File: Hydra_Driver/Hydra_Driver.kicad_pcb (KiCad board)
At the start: 2 copper layers, 58 x 42 mm, 99 parts, among them IC101 ESP32-S3-WROOM-1-N4, IC201 DRV8313RHHR, IC301 DRV8313RHHR, J101 USB4105-GF-A, J102 Conn_01x02, J103 Conn_01x07, J104 Conn_01x04, J105 Conn_01x03, J107 Conn_01x04, J108 Conn_01x03, J109 Conn_01x02, J110 Conn_01x07, SW101 SW_SPST, SW102 SW_SPST, U101 USBLC6-2SC6, U102 MIC5504-3.3YM5-TR, U103 SN74LVC1G80DBVR, U201 INA4181A2IPWR, U301 INA4181A2IPWR

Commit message: Added thermal vias to driver pads
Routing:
- net GND: track 167.0 -> 170.9 mm, vias 65 -> 73
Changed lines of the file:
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@@
+	)
+	(segment
+		(start 43.66 18.89)
+		(end 44.02 19.25)
+		(width 0.2)
+		(layer "F.Cu")
+		(net 1)
 	)
 	(segment
@@
 	)
 	(segment
+		(start 42.1 19.25)
+		(end 43.3 19.25)
+		(width 0.2)
+		(layer "F.Cu")
+		(net 1)
+	)
+	(segment
 		(start 55.4625 24.75)
 		(end 54.603 24.75)
@@
 	)
 	(segment
+		(start 44.168191 19.25)
+		(end 45.168191 20.25)
+		(width 0.2)
+		(layer "F.Cu")
+		(net 1)
+	)
+	(segment
 		(start 20.5 28.5)
 		(end 20.18 28.82)
@@
 	)
 	(segment
+		(start 46.4 21.6)
+		(end 46.69 21.31)
+		(width 0.2)
+		(layer "F.Cu")
+		(net 1)
+	)
+	(segment
+		(start 46 19.25)
+		(end 45.725 19.525)
+		(width 0.2)
+		(layer "F.Cu")
+		(net 1)
+	)
+	(segment
 		(start 20.18 13.43)
 		(end 20.5 13.75)
@@
 		(start 54.5 15.5)
 		(end 54.75 15.25)
+		(width 0.2)
+		(layer "F.Cu")
+		(net 1)
+	)
+	(segment
+		(start 43.5 19.75)
+		(end 44.5 19.75)
 		(width 0.2)
 		(layer "F.Cu")
@@
 	)
 	(segment
+		(start 46.35 21.6)
+		(end 45 20.25)
+		(width 0.2)
+		(layer "F.Cu")
+		(net 1)
+	)
+	(segment
 		(start 54.889 31.389)
 		(end 54.3 30.8)
@@
 	)
 	(segment
-		(start 46.5 17.35)
-		(end 46.5 18.75)
+		(start 44.02 19.25)
+		(end 44.168191 19.25)
 		(width 0.2)
 		(layer "F.Cu")
@@
 	(segment
 		(start 42.1 19.75)
-		(end 44.5 19.75)
+		(end 43.5 19.75)
 		(width 0.2)
 		(layer "F.Cu")
@@
 	)
 	(segment
+		(start 46.39 18.86)
+		(end 46.5 18.75)
+		(width 0.2)
+		(layer "F.Cu")
+		(net 1)
+	)
+	(segment
 		(start 54.3 30.8)
 		(end 54.3 30)
@@
 	)
 	(segment
+		(start 46.39 18.88)
+		(end 46.39 18.55)
+		(width 0.2)
+		(layer "F.Cu")
+		(net 1)
+	)
+	(segment
 		(start 54.603 24.75)
 		(end 54.603 24.2517)
@@
 	)
 	(segment
-		(start 46 19.25)
-		(end 45 20.25)
-		(width 0.2)
-		(layer "F.Cu")
-		(net 1)
-	)
-	(segment
 		(start 29.239728 34.85267)
 		(end 29.6174 34.474998)
@@
 	)
 	(segment
+		(start 46.5 18.44)
+		(end 46.5 17.35)
+		(width 0.2)
+		(layer "F.Cu")
+		(net 1)
+	)
+	(segment
 		(start 29.101415 34.85267)
 		(end 29.239728 34.85267)
@@
 		(start 36.9046 1.49)
 		(end 36.9046 0.9)
-		(width 0.2)
-		(layer "F.Cu")
-		(net 1)
-	)
-	(segment
-		(start 44 19.25)
-		(end 45 20.25)
 		(width 0.2)
 		(layer "F.Cu")
@@
 	)
 	(segment
+		(start 46.69 18.94)
+		(end 46.5 18.75)
+		(width 0.2)
+		(layer "F.Cu")
+		(net 1)
+	)
+	(segment
 		(start 46.5 16.50826)
 		(end 46.49587 16.50413)
@@
 	)
 	(segment
+		(start 46.39 18.88)
+		(end 46.39 18.86)
+		(width 0.2)
+		(layer "F.Cu")
+		(net 1)
+	)
+	(segment
 		(start 54.6 19.4)
 		(end 54.75 19.25)
@@
 	)
 	(segment
-		(start 46.5 18.75)
-		(end 45 20.25)
-		(width 0.2)
-		(layer "F.Cu")
-		(net 1)
-	)
-	(segment
 		(start 49.25 27.4)
 		(end 50.15 27.4)
@@
 	)
 	(segment
+		(start 46.4 21.6)
+		(end 46.35 21.6)
+		(width 0.2)
+		(layer "F.Cu")
+		(net 1)
+	)
+	(segment
 		(start 56 39.6)
 		(end 56.029 39.629)
@@
 	)
 	(segment
+		(start 43.3 19.25)
+		(end 43.66 18.89)
+		(width 0.2)
+		(layer "F.Cu")
+		(net 1)
+	)
+	(segment
+		(start 45.725 19.525)
+		(end 45 20.25)
+		(width 0.2)
+		(layer "F.Cu")
+		(net 1)
+	)
+	(segment
 		(start 10.62 17.244033)
 		(end 11.002 17.626033)
@@
 		(start 7 30)
 		(end 6.6 30.4)
-		(width 0.2)
-		(layer "F.Cu")
-		(net 1)
-	)
-	(segment
-		(start 42.1 19.25)
-		(end 44 19.25)
 		(width 0.2)
 		(layer "F.Cu")
@@
 	)
 	(segment
+		(start 45.168191 20.25)
+		(end 45 20.25)
+		(width 0.2)
+		(layer "F.Cu")
+		(net 1)
+	)
+	(segment
 		(start 57.699 24.199)
 		(end 57.699 26.311)
@@
 	)
 	(segment
+		(start 46.69 21.31)
+		(end 46.69 18.94)
+		(width 0.2)
+		(layer "F.Cu")
+		(net 1)
+	)
+	(segment
 		(start 52.9485 4.249999)
 		(end 51.5 4.25)
@@
 	)
 	(segment
+		(start 46.39 18.55)
+		(end 46.5 18.44)
+		(width 0.2)
+		(layer "F.Cu")
+		(net 1)
+	)
+	(segment
 		(start 5 23.214013)
 		(end 5.114013 23.1)
@@
 	(via
 		(at 48.335707 6.334293)
+		(size 0.6)
+		(drill 0.3)
+		(layers "F.Cu" "B.Cu")
+		(net 1)
+	)
+	(via
+		(at 46.26 32.3)
 		(size 0.6)
 		(drill 0.3)
@@
 	)
 	(via
+		(at 46.39 18.88)
+		(size 0.6)
+		(drill 0.3)
+		(layers "F.Cu" "B.Cu")
+		(net 1)
+	)
+	(via
 		(at 50.5 14.5)
 		(size 0.6)
@@
 	)
 	(via
+		(at 43.66 18.89)
+		(size 0.6)
+		(drill 0.3)
+		(layers "F.Cu" "B.Cu")
+		(net 1)
+	)
+	(via
 		(at 13.75 13.5)
 		(size 0.6)
@@
 	(via
 		(at 50.25 27.5)
+		(size 0.6)
+		(drill 0.3)
+		(layers "F.Cu" "B.Cu")
+		(net 1)
+	)
+	(via
+		(at 43.69 34.98)
 		(size 0.6)
 		(drill 0.3)
@@
 	)
 	(via
+		(at 46.28 34.92)
+		(size 0.6)
+		(drill 0.3)
+		(layers "F.Cu" "B.Cu")
+		(net 1)
+	)
+	(via
 		(at 50 8.25)
 		(size 0.6)
@@
 	(via
 		(at 36.6 40.4)
+		(size 0.6)
+		(drill 0.3)
+		(layers "F.Cu" "B.Cu")
+		(net 1)
+	)
+	(via
+		(at 46.4 21.6)
 		(size 0.6)
 		(drill 0.3)
@@
 		(size 0.6)
 		(drill 0.3)
+		(layers "F.Cu" "B.Cu")
+		(net 1)
+	)
+	(via
+		(at 43.64 21.66)
+		(size 0.6)
+		(drill 0.3)
+		(layers "F.Cu" "B.Cu")
+		(net 1)
+	)
+	(via
+		(at 43.7 32.36)
+		(size 0.6)
+		(drill 0.3)

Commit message: Incorporated design review feedback and updated fab files
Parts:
- C203, C204, C205, C303, C304, C305: value 1n -> 22n
- R201, R202, R203, R204, R205, R206, R301, R302, R303, R304, R305, R306: value 47 -> 10
- U201, U301: value INA4181A2IPWR -> INA4181A3IPWR
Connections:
- C208 pad 2: +3.3V -> /Driver_Unit/L3V3
- C210 pad 2: +3.3V -> /Driver_Unit/L3V3
- C308 pad 2: +3.3V -> /Driver_Unit1/L3V3
- C310 pad 2: +3.3V -> /Driver_Unit1/L3V3
- IC201 pad 25: +3.3V -> /Driver_Unit/L3V3
- IC301 pad 25: +3.3V -> /Driver_Unit1/L3V3
- R207 pad 2: +3.3V -> /Driver_Unit/L3V3
- R208 pad 2: +3.3V -> /Driver_Unit/L3V3
- R209 pad 2: +3.3V -> /Driver_Unit/L3V3
- R210 pad 2: +3.3V -> /Driver_Unit/L3V3
- R307 pad 2: +3.3V -> /Driver_Unit1/L3V3
- R308 pad 2: +3.3V -> /Driver_Unit1/L3V3
- R309 pad 2: +3.3V -> /Driver_Unit1/L3V3
- R310 pad 2: +3.3V -> /Driver_Unit1/L3V3
- U201 pad 5: +3.3V -> /Driver_Unit/L3V3
- U301 pad 5: +3.3V -> /Driver_Unit1/L3V3
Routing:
- net +3.3V: track 161.3 -> 113.0 mm, vias 8 -> 5
- net /Driver_Unit1/L3V3: track 0.00 -> 27.9 mm, vias 0 -> 2
- net /Driver_Unit/L3V3: track 0.00 -> 25.0 mm, vias 0 -> 2
- net /IN1A: track 13.7 -> 14.7 mm
- net /SENSE1A: track 13.6 -> 12.8 mm
- net /GPIO0: track 24.7 -> 25.4 mm
- net /SDA1: track 21.2 -> 21.8 mm
- net VMOT: track 177.6 -> 177.1 mm
- net GND: track 170.9 -> 171.2 mm, vias 73 -> 80
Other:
- board text added: "Hydra V2 ©CGR"

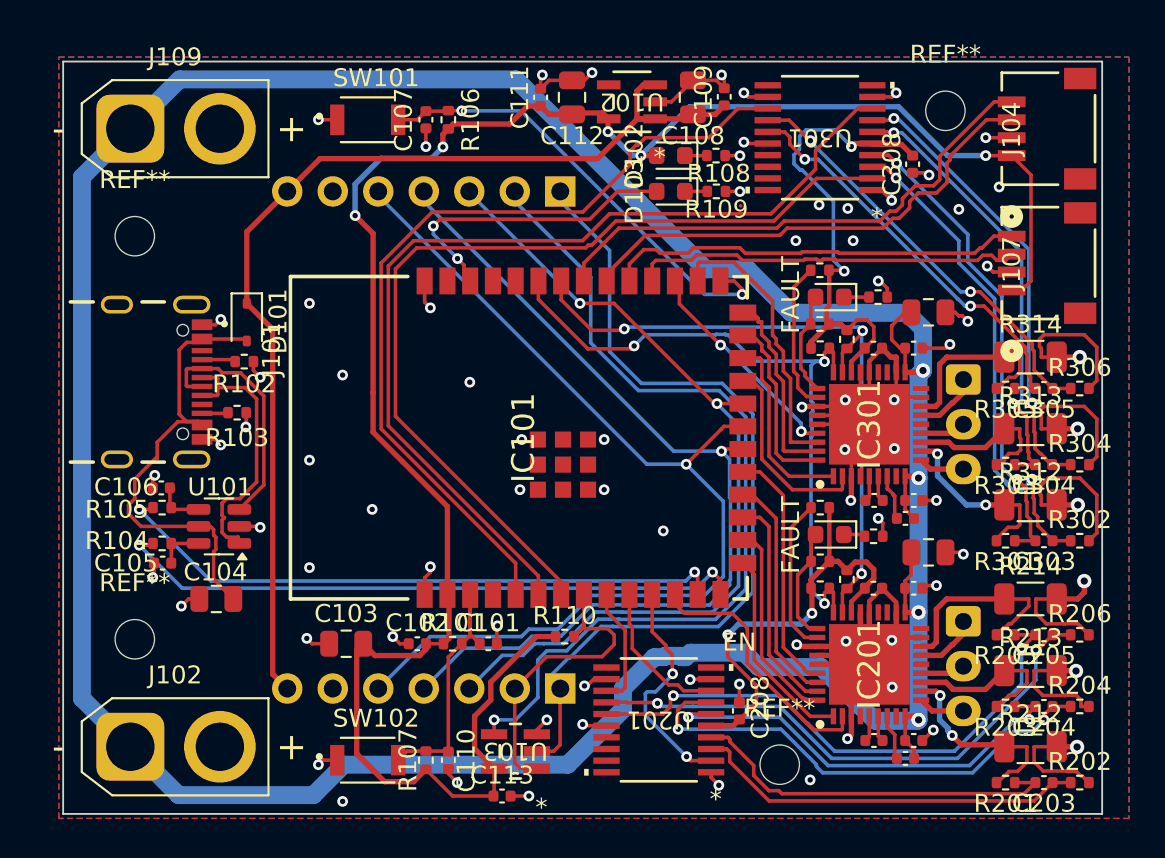
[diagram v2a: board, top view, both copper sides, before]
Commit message: Fixed issues preparing for build
Fixed XT30 connectors on Hydra_Driver reversed, fixed I2C connector pin order, refined silkscreens
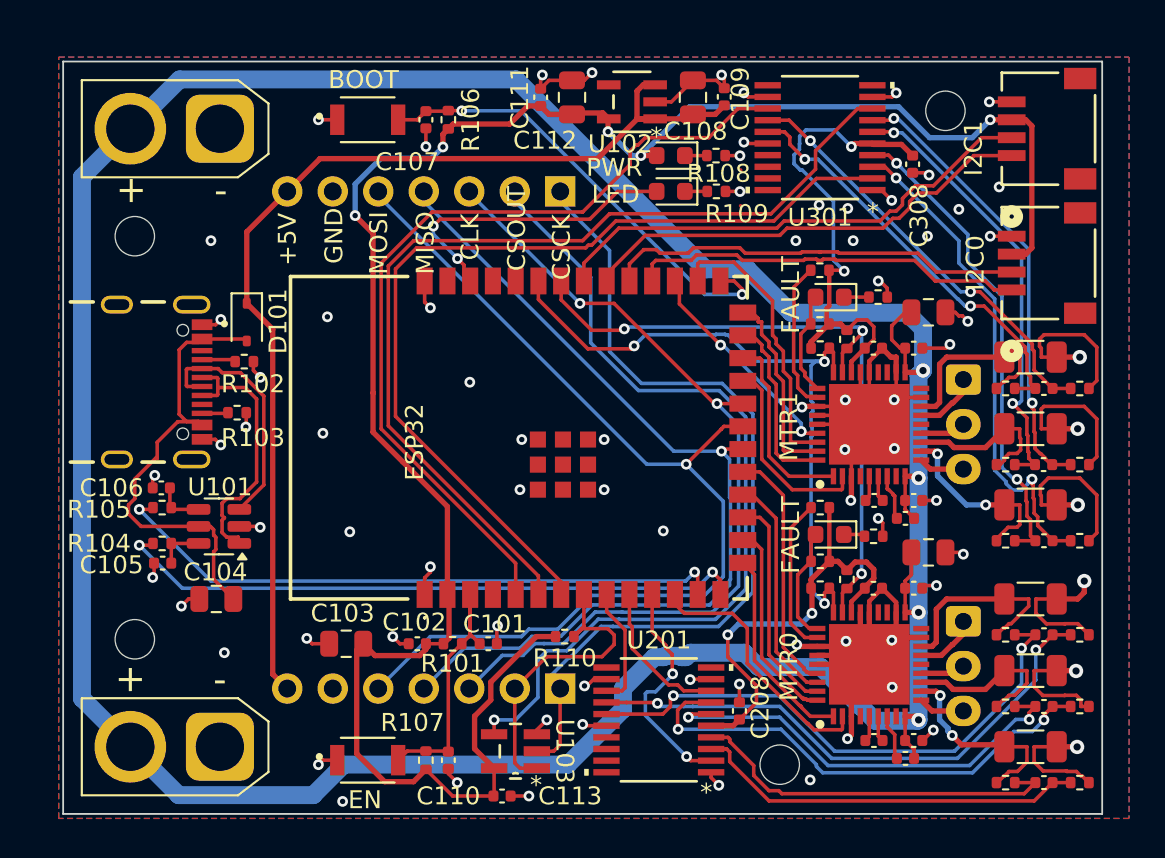
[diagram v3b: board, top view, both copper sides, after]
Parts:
- moved J102 5.00 mm to (8.75, 38.2), turned to 180 degrees
- moved J109 5.00 mm to (8.75, 3.75), turned to 180 degrees
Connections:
- IC101 pad 30: /SDA1 -> /SCL1
- IC101 pad 31: /SCL1 -> /SDA1
- IC101 pad 32: /SDA2 -> /SCL2
- IC101 pad 33: /SCL2 -> /SDA2
- J102 pad 1: VMOT -> GND
- J102 pad 2: GND -> VMOT
- J104 pad 1: +3.3V -> /SCL2
- J104 pad 2: GND -> /SDA2
- J104 pad 3: /SDA2 -> +3.3V
- J104 pad 4: /SCL2 -> GND
- J107 pad 1: +3.3V -> /SCL1
- J107 pad 2: GND -> /SDA1
- J107 pad 3: /SDA1 -> +3.3V
- J107 pad 4: /SCL1 -> GND
- J109 pad 1: VMOT -> GND
- J109 pad 2: GND -> VMOT
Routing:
- net /SCL2: track 29.6 -> 25.9 mm
- net /SDA1: track 21.8 -> 23.5 mm
- net /SCL1: track 23.4 -> 22.2 mm
- net +3.3V: track 113.0 -> 113.6 mm
- net GND: track 171.2 -> 170.7 mm, vias 80 -> 81
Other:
- board text added: "+5V"
- board text added: "BOOT"
- board text added: "CLK"
- board text added: "CSCK"
- board text added: "CSIN"
- board text added: "CSOUT"
- board text added: "ESP32"
- board text added: "I2C0"
- board text added: "LED"
- board text added: "MISO"
- board text added: "MOSI"
- board text added: "MTR0"
- board text added: "MTR1"
- board text added: "PWR"
- board text removed: "+3.3"
